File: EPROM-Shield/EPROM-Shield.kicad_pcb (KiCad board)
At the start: 2 copper layers, 63.5 x 54.6 mm, 21 parts, among them J1 Conn_01x07, J2 Conn_01x06, J3 Conn_01x08, J4 Conn_01x06, U1 74LS595, U2 74LS595, U3 28C256

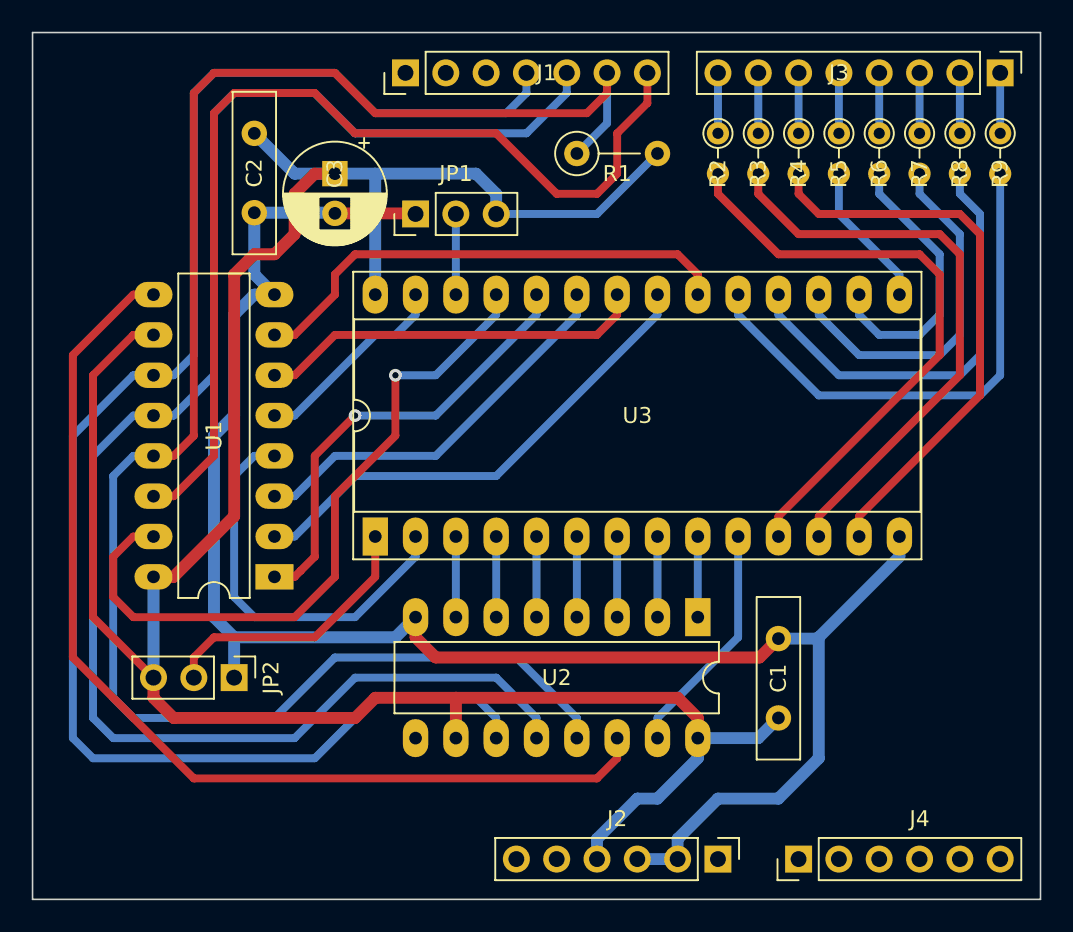
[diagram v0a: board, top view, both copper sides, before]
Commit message: EPROM-Shield: add GND fill zones
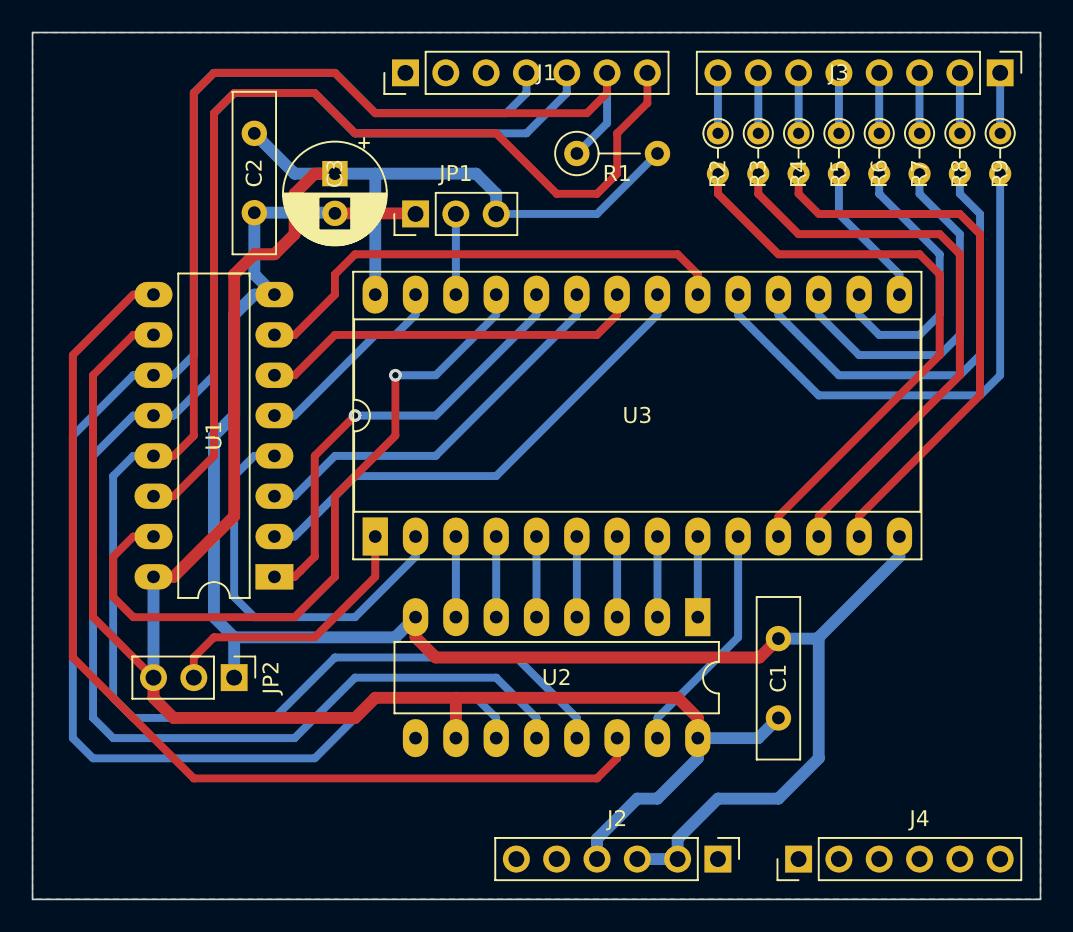
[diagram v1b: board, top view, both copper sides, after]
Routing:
- added copper zone on B.Cu, net GND
- added copper zone on F.Cu, net GND
